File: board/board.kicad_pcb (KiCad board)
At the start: 2 copper layers, 58.1 x 29.5 mm, 41 parts, among them J2 Conn_01x10, J3 Conn_01x06, J4 Conn_01x02, J7 Conn_01x30, J8 USB_C_Receptacle_USB2.0_16P, J9 Conn_01x02, U2 nPM1300-QEAA, U3 MDBT50Q-P1MV2, U4 TVS_Array, Y1 32k Hz

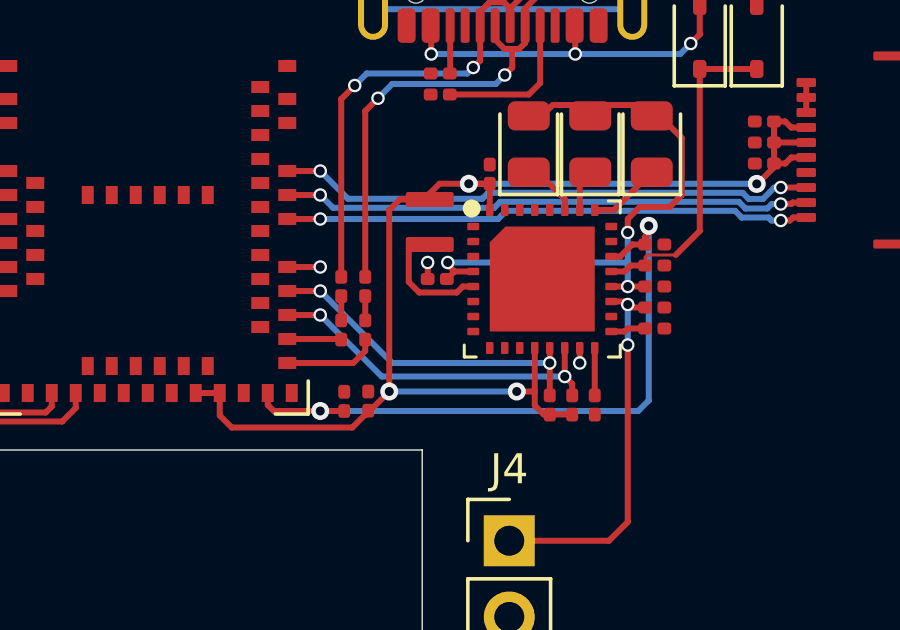
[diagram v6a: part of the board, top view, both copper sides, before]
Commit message: board: pcb route shphld
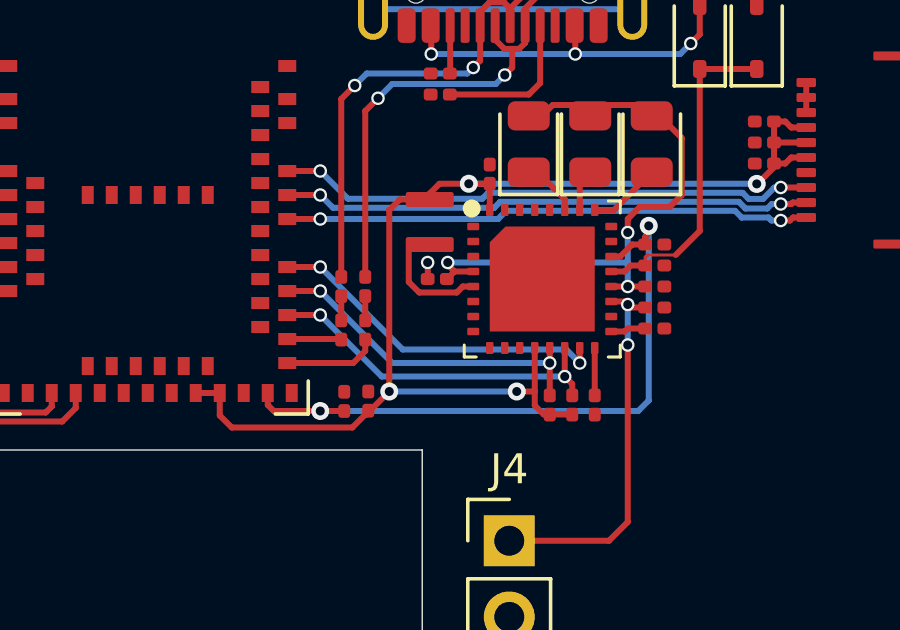
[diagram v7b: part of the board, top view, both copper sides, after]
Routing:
- net shphld: track 1.60 -> 11.6 mm
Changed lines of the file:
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@@
+	)
+	(segment
+		(start 113.8 63.65)
+		(end 114.25 64.1)
+		(width 0.2)
+		(layer "B.Cu")
+		(net 35)
+	)
+	(segment
+		(start 105.6 60.9)
+		(end 108.35 63.65)
+		(width 0.2)
+		(layer "B.Cu")
+		(net 35)
+	)
+	(segment
+		(start 108.35 63.65)
+		(end 113.8 63.65)
+		(width 0.2)
+		(layer "B.Cu")
+		(net 35)
 	)
 	(segment
@@
 	)
 	(segment
+		(start 107.9 65.05)
+		(end 112.15 65.05)
+		(width 0.2)
+		(layer "B.Cu")
+		(net 46)
+	)
+	(segment
 		(start 110.55 58.125)
 		(end 120.125 58.125)
@@
 		(width 0.2)
 		(layer "B.Cu")
-		(net 46)
-	)
-	(segment
-		(start 107.9 65.05)
-		(end 112.15 65.05)
-		(width 0.2)
-		(layer "B.Cu")

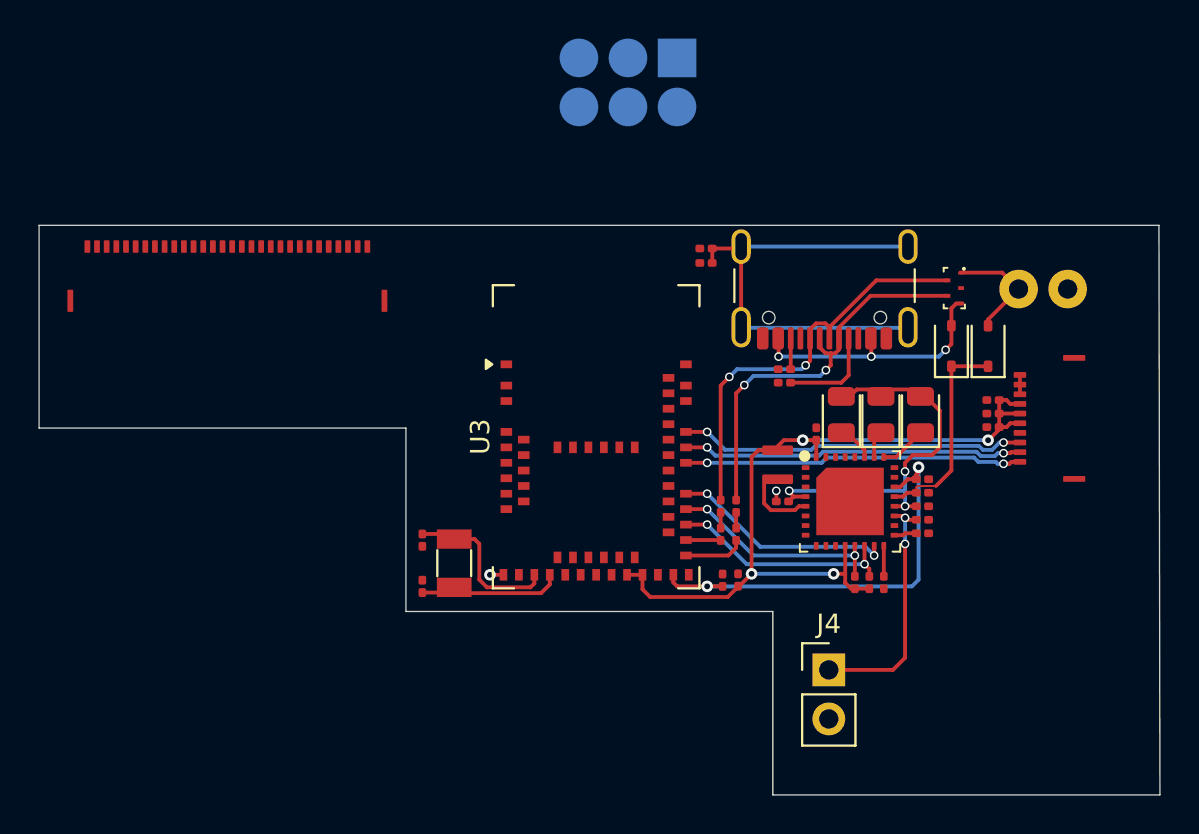
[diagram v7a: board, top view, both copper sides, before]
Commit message: board: pcb route bottom front keys
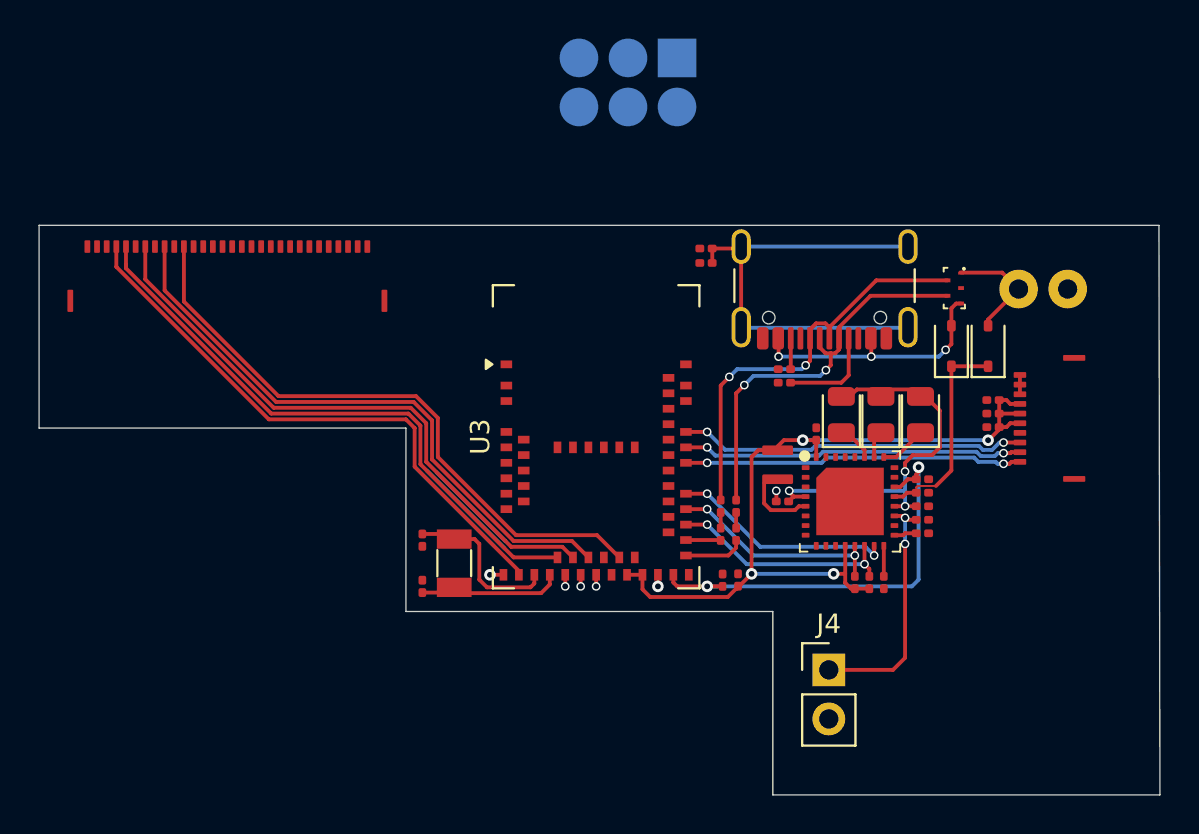
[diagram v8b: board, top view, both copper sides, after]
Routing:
- net key8: track 0.00 -> 32.1 mm
- net key6: track 0.00 -> 31.1 mm
- net key4: track 0.00 -> 31.0 mm
- net key2: track 0.00 -> 30.9 mm
- net key1: track 0.00 -> 29.8 mm
- net key5: track 0.00 -> 6.35 mm, vias 0 -> 1
- net key3: track 0.00 -> 6.25 mm, vias 0 -> 1
- net key7: track 0.00 -> 5.66 mm, vias 0 -> 1
- net +1V8: track 0.00 -> 0.60 mm, vias 0 -> 1
